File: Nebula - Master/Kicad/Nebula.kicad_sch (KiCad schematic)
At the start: 91 parts, among them J1 1054550101, J2 Display, M1 HMotor, Q1 s8050, Q2 C70022, Q3 s8050, SW1 SW_Push, SW2 SW_Push, SW3 SW_Push, U1 DRV5021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

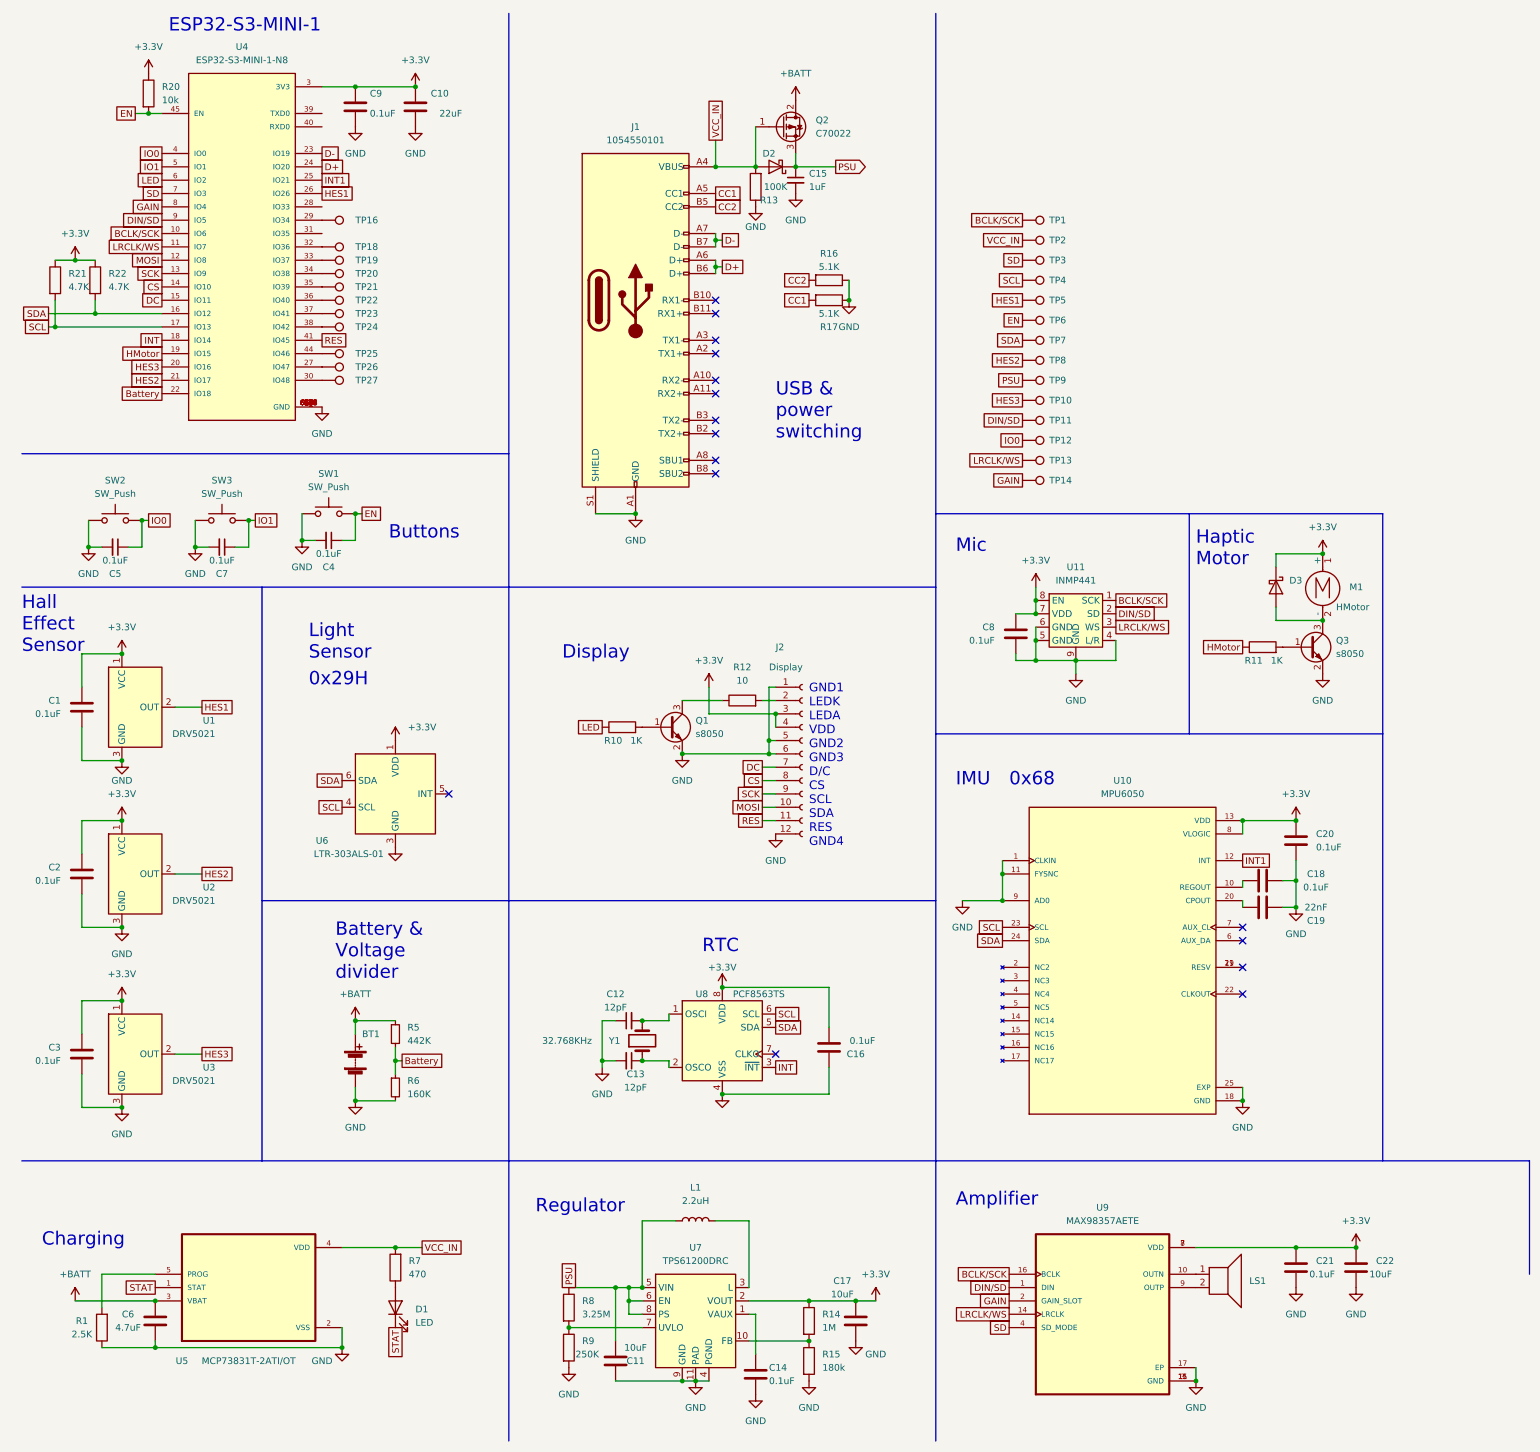
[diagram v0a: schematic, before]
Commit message: Added BOM and minor changes
Fixed mosfet footprint and magnetic sensor footprints
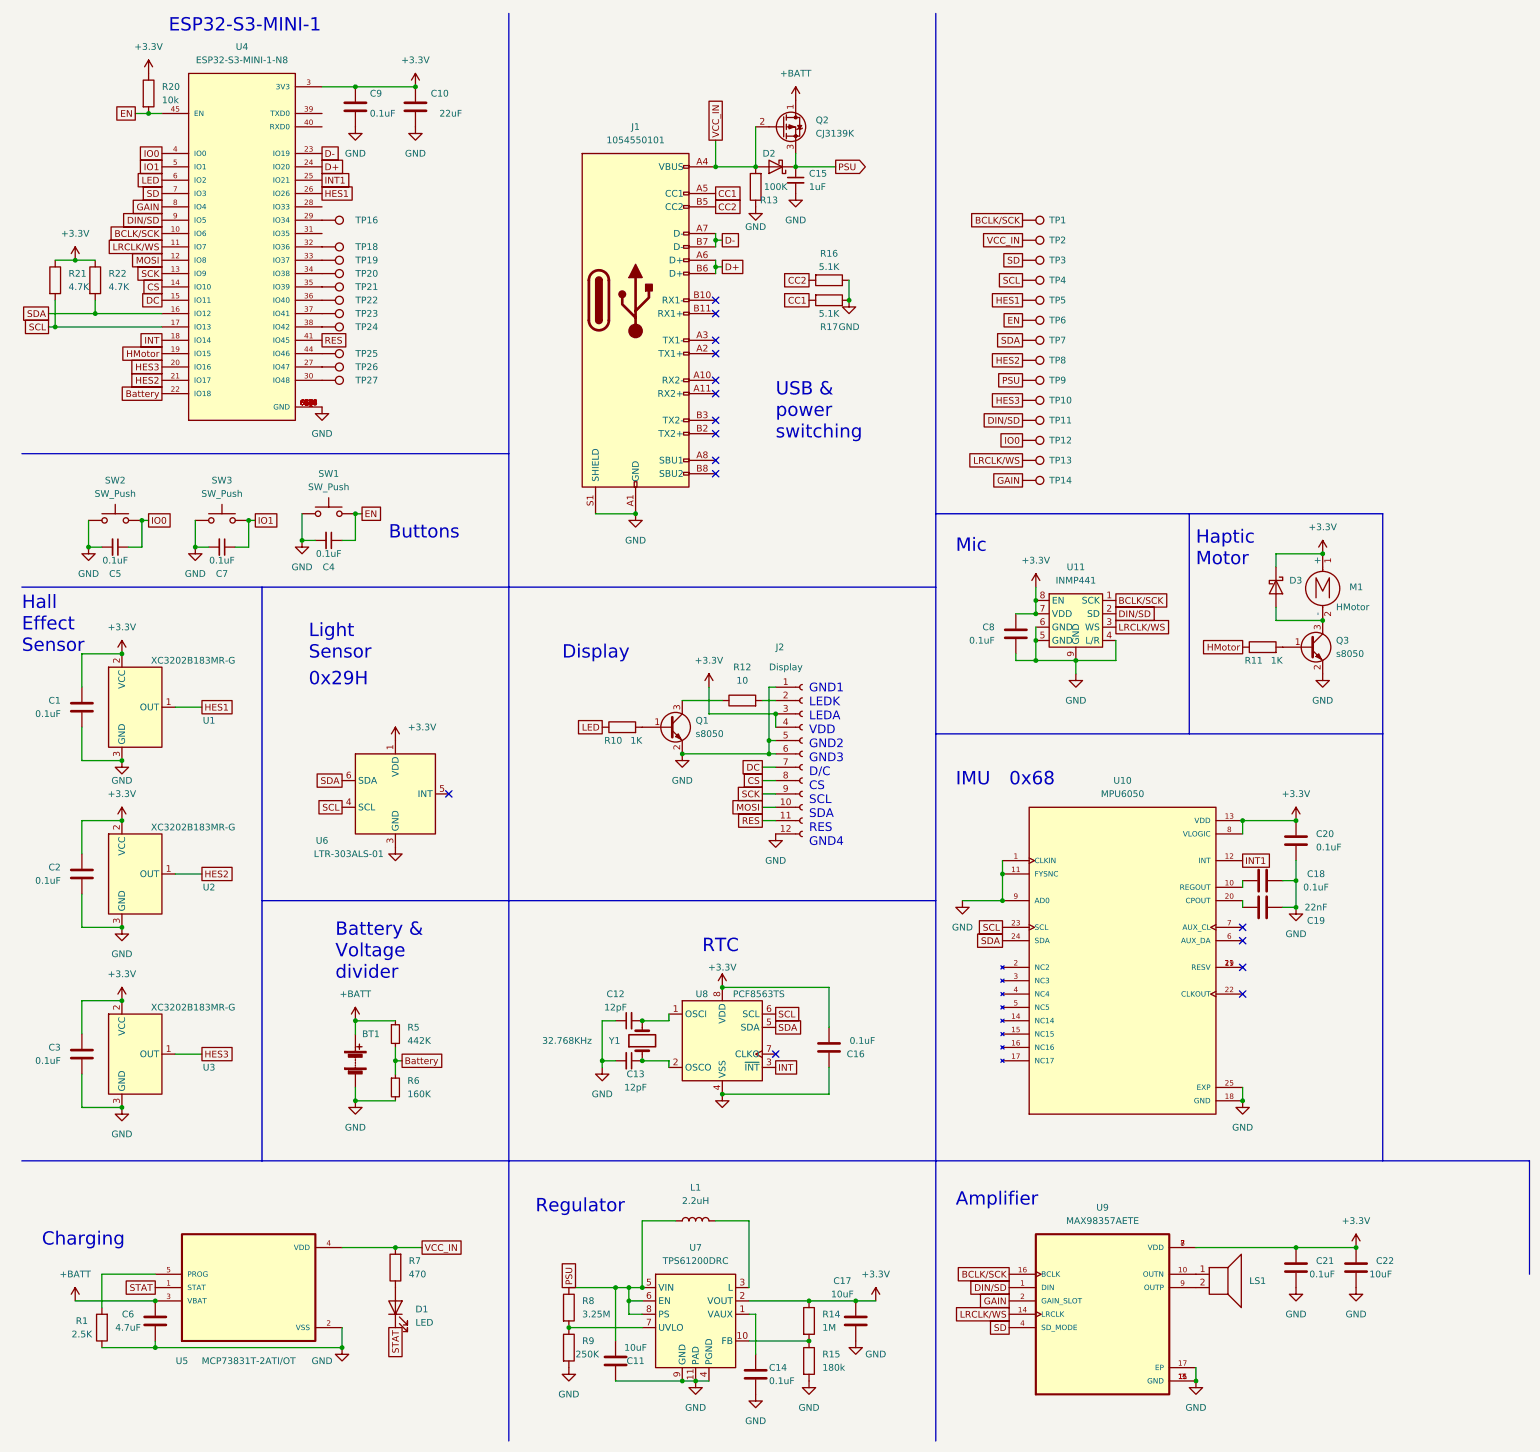
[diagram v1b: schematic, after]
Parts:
- removed Q2: C70022, Package_TO_SOT_SMD:SOT-723, symbol Device:Q_PMOS_GDS
- added Q2: CJ3139K, Package_TO_SOT_SMD:SOT-723, symbol Device:Q_PMOS_DGS
- C1, C14, C16, C18, C2, C20, C21, C3, C4, C5, C7, C8, C9: LCSC (none) -> C123453
- C10: LCSC (none) -> C415703
- C11, C17, C22: LCSC (none) -> C15525
- C13: LCSC (none) -> C696888
- C15: LCSC (none) -> C14445
- C19: LCSC (none) -> C380305
- C6: LCSC (none) -> C87147
- D2, D3: LCSC (none) -> C143773
- L1: LCSC (none) -> C86092
- M1: LCSC (none) -> C2895081
- Q1, Q3: LCSC (none) -> C779775
- R1: LCSC (none) -> C2692758
- R10, R11: LCSC (none) -> C242161
- R12: LCSC (none) -> C413044
- R13: LCSC (none) -> C413017
- R14: LCSC (none) -> C413126
- R15: LCSC (none) -> C2909325
- R16, R17: LCSC (none) -> C328327
- R20: LCSC (none) -> C278577
- R21, R22: LCSC (none) -> C2906869
- R5: LCSC (none) -> C409854
- R6: LCSC (none) -> C273339
- R7: LCSC (none) -> C284584
- R8: LCSC (none) -> C227048
- R9: LCSC (none) -> C2998084
- U1, U2, U3: value DRV5021 -> XC3202B183MR-G
- U4: LCSC  (none) -> C2913206
- U5: LCSC (none) -> C14879
- U6: LCSC (none) -> C364577
- U7: LCSC (none) -> C140320
- U9: Availability Unavailable -> (none); LCSC (none) -> C910544; Package TQFN-16 Maxim -> (none)
- Y1: LCSC (none) -> C383844
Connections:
- net +3V3: now also U1.2 (VCC), U2.2 (VCC), U3.2 (VCC); no longer U1.1 (VCC), U2.1 (VCC), U3.1 (VCC)
- net +BATT: now also Q2.1 (D)
- net HES1: now also U1.1 (OUT); no longer U1.2 (OUT)
- net HES2: now also U2.1 (OUT); no longer U2.2 (OUT)
- net HES3: now also U3.1 (OUT); no longer U3.2 (OUT)
- net PSU: now also Q2.3 (S)
- net VCC_IN: now also Q2.2 (G)
